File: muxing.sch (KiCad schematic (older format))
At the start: 10 parts, among them J10 Conn_01x06, J11 Conn_01x06

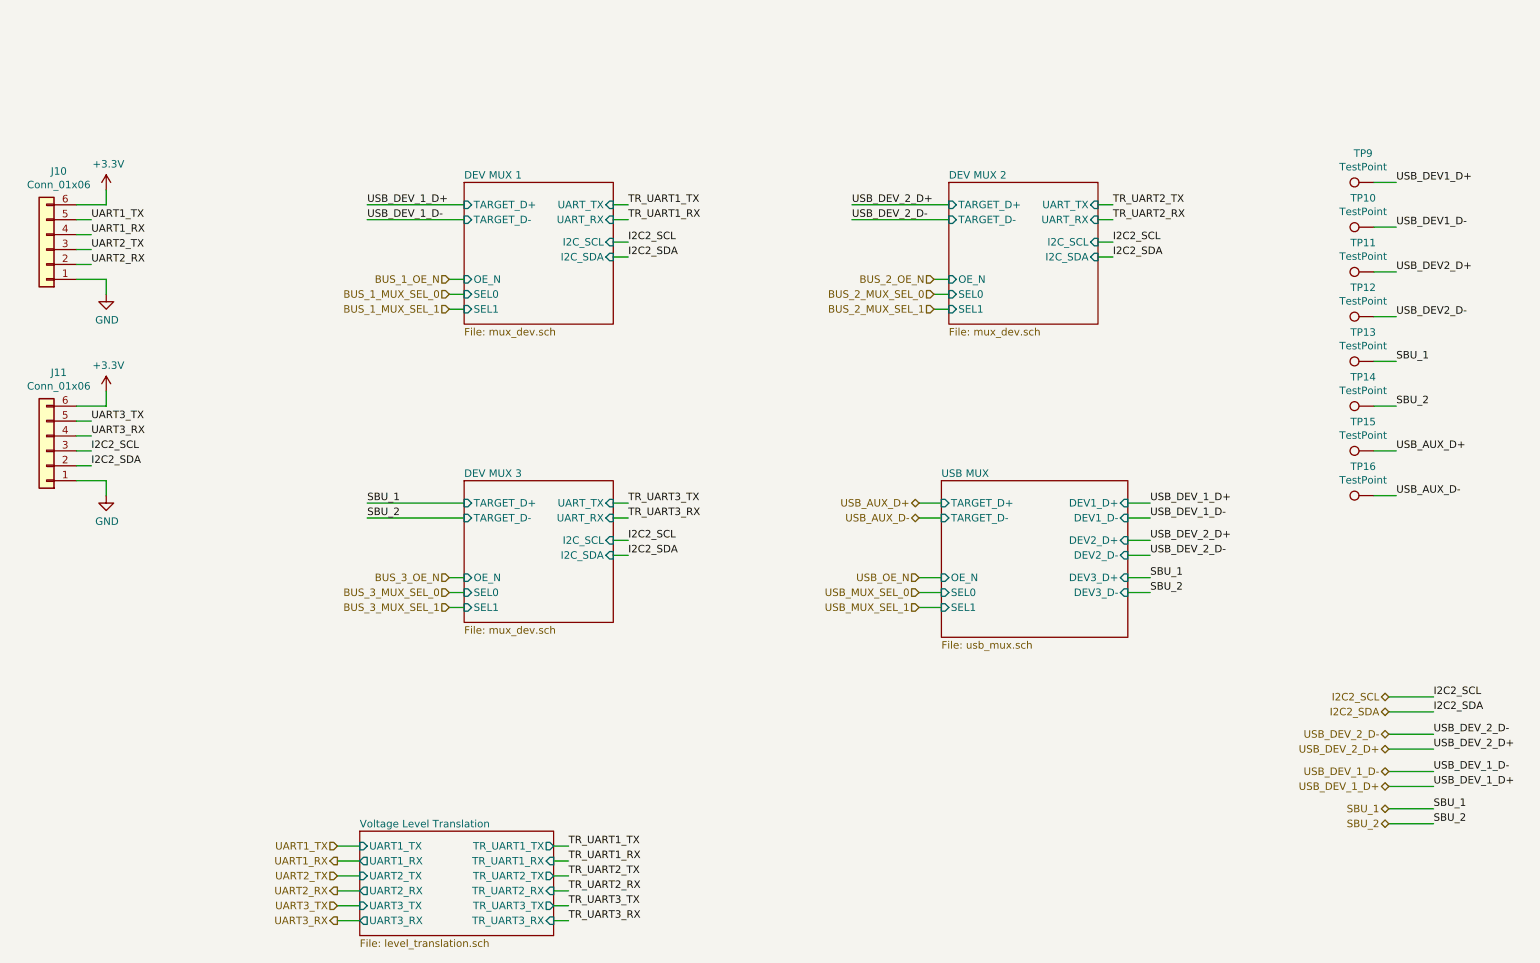
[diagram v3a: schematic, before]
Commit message: Replace MCU by something available in distributors
Given the current chip shortage the STM32F0 was not available from
JLCPCB. This one (STM32F411CE) is available in large quantities from
JLCPCB. Despite being much more powerful than the F0, it is still in the
price range and actually cheaper than the STM32F103C8T6... which I don't
understand...
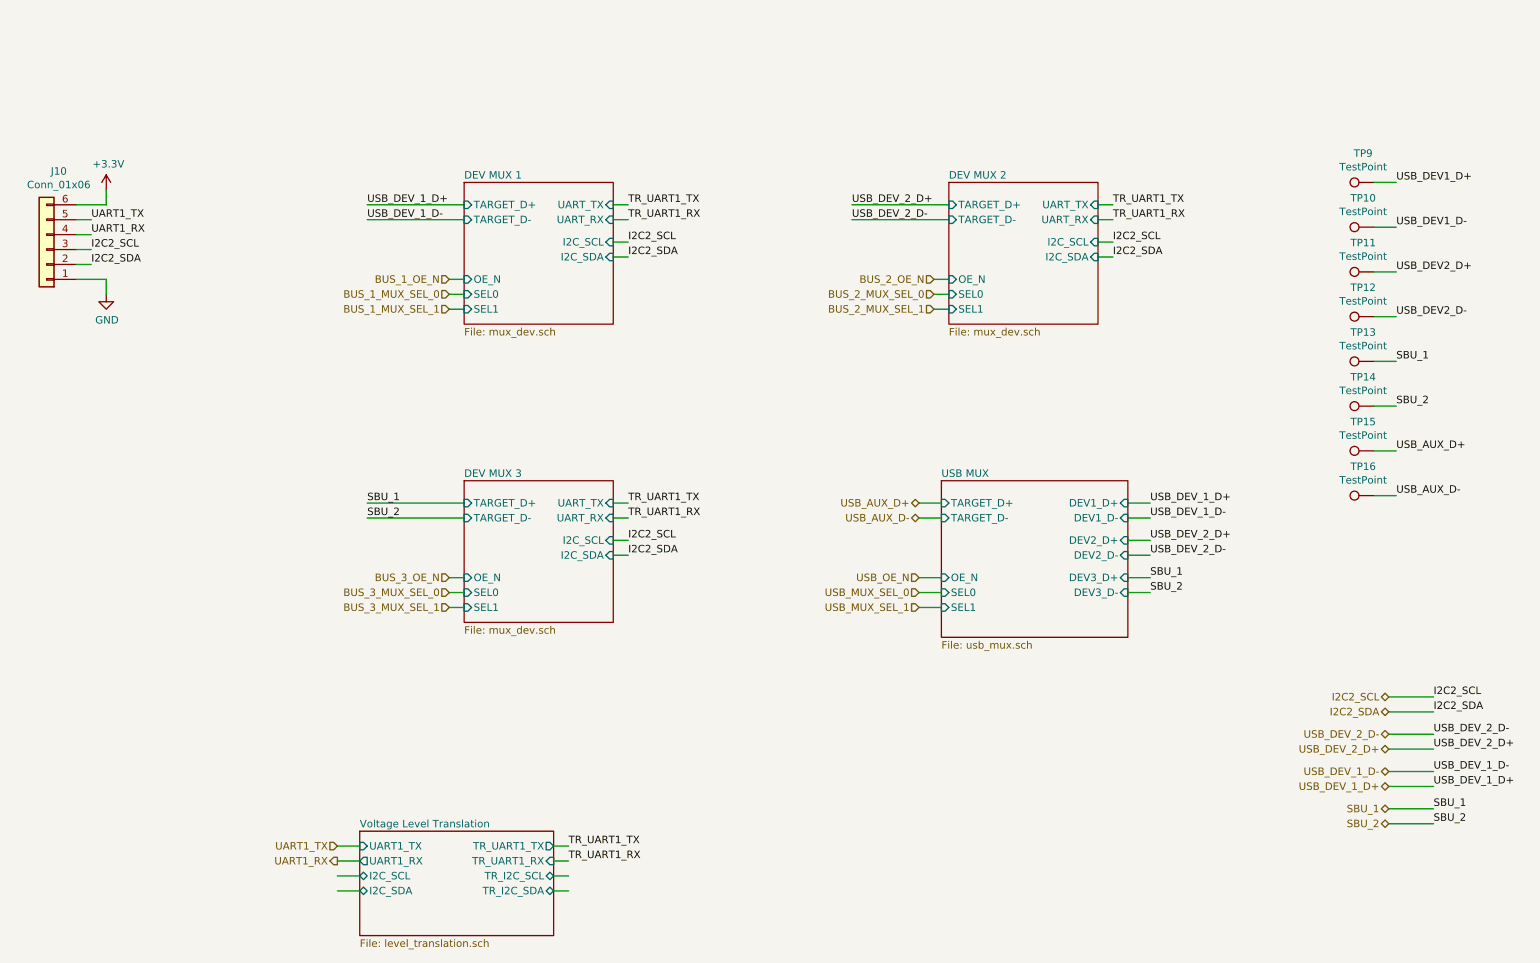
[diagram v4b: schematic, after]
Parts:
- removed J11: Conn_01x06, symbol Connector_Generic:Conn_01x06
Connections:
- net labels removed: TR_UART2_RX, TR_UART2_TX, TR_UART3_RX, TR_UART3_TX, UART2_RX, UART2_TX, UART3_RX, UART3_TX
- wire segments 82 -> 70
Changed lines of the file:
@@
 Wire Wire Line
 	7100 2250 6450 2250
-Text Label 8200 2150 0    50   ~ 0
-TR_UART2_TX
-Text Label 8200 2250 0    50   ~ 0
-TR_UART2_RX
 Wire Wire Line
 	8100 2150 8200 2150
@@
 Wire Wire Line
 	3850 4250 3200 4250
-Text Label 4950 4150 0    50   ~ 0
-TR_UART3_TX
-Text Label 4950 4250 0    50   ~ 0
-TR_UART3_RX
 Wire Wire Line
 	4850 4150 4950 4150
@@
 Text Label 4550 6550 0    50   ~ 0
 TR_UART1_RX
-Text Label 4550 6650 0    50   ~ 0
-TR_UART2_TX
-Text Label 4550 6750 0    50   ~ 0
-TR_UART2_RX
-Text Label 4550 6850 0    50   ~ 0
-TR_UART3_TX
-Text Label 4550 6950 0    50   ~ 0
-TR_UART3_RX
 Text HLabel 3750 4850 0    50   Input ~ 0
 BUS_3_MUX_SEL_1
@@
 F2 "UART1_TX" I L 3150 6450 50
 F3 "UART1_RX" O L 3150 6550 50
-F4 "UART2_TX" I L 3150 6650 50
-F5 "UART2_RX" O L 3150 6750 50
-F6 "UART3_TX" I L 3150 6850 50
-F7 "UART3_RX" O L 3150 6950 50
-F8 "TR_UART1_TX" O R 4450 6450 50
-F9 "TR_UART1_RX" I R 4450 6550 50
-F10 "TR_UART2_TX" O R 4450 6650 50
-F11 "TR_UART2_RX" I R 4450 6750 50
-F12 "TR_UART3_TX" O R 4450 6850 50
-F13 "TR_UART3_RX" I R 4450 6950 50
+F4 "TR_UART1_TX" O R 4450 6450 50
+F5 "TR_UART1_RX" I R 4450 6550 50
+F6 "I2C_SCL" B L 3150 6650 50
+F7 "I2C_SDA" B L 3150 6750 50
+F8 "TR_I2C_SCL" B R 4450 6650 50
+F9 "TR_I2C_SDA" B R 4450 6750 50
 $EndSheet
 Wire Wire Line
@@
 Wire Wire Line
 	4550 6750 4450 6750
-Wire Wire Line
-	4450 6850 4550 6850
-Wire Wire Line
-	4550 6950 4450 6950
 $Sheet
 S 7050 4000 1250 1050
@@
 Text HLabel 3000 6550 0    50   Output ~ 0
 UART1_RX
-Text HLabel 3000 6650 0    50   Input ~ 0
-UART2_TX
-Text HLabel 3000 6750 0    50   Output ~ 0
-UART2_RX
-Text HLabel 3000 6850 0    50   Input ~ 0
-UART3_TX
-Text HLabel 3000 6950 0    50   Output ~ 0
-UART3_RX
 Wire Wire Line
 	3000 6450 3150 6450
@@
 Wire Wire Line
 	3150 6750 3000 6750
-Wire Wire Line
-	3000 6850 3150 6850
-Wire Wire Line
-	3150 6950 3000 6950
 Text HLabel 6900 4150 0    50   BiDi ~ 0
 USB_AUX_D+
@@
 Text Label 1350 2350 0    50   ~ 0
 UART1_RX
-Text Label 1350 2450 0    50   ~ 0
-UART2_TX
-Text Label 1350 2550 0    50   ~ 0
-UART2_RX
-Text Label 1350 3600 0    50   ~ 0
-UART3_TX
-Text Label 1350 3700 0    50   ~ 0
-UART3_RX
 $Comp
 L power:+3.3V #PWR019
@@
 	1250 2550 1350 2550
 Wire Wire Line
-	1350 3600 1250 3600
-Wire Wire Line
-	1250 3700 1350 3700
-Wire Wire Line
 	1250 2650 1450 2650
 Wire Wire Line
@@
 Wire Wire Line
 	1450 2150 1250 2150
-$Comp
-L power:+3.3V #PWR023
-U 1 1 61A3EEDE
-P 1450 3400
-F 0 "#PWR023" H 1450 3250 50  0001 C CNN
-F 1 "+3.3V" H 1465 3573 50  0000 C CNN
-F 2 "" H 1450 3400 50  0001 C CNN
-F 3 "" H 1450 3400 50  0001 C CNN
-	1    1450 3400
-	1    0    0    -1
-$EndComp
-$Comp
-L power:GND #PWR025
-U 1 1 61A3EEE4
-P 1450 4100
-F 0 "#PWR025" H 1450 3850 50  0001 C CNN
-F 1 "GND" H 1455 3927 50  0000 C CNN
-F 2 "" H 1450 4100 50  0001 C CNN
-F 3 "" H 1450 4100 50  0001 C CNN
-	1    1450 4100
-	1    0    0    -1
-$EndComp
-Wire Wire Line
-	1250 4000 1450 4000
-Wire Wire Line
-	1450 4000 1450 4100
-Wire Wire Line
-	1450 3400 1450 3500
-Wire Wire Line
-	1450 3500 1250 3500
-$Comp
-L Connector_Generic:Conn_01x06 J11
-U 1 1 61A4FE69
-P 1050 3800
-F 0 "J11" H 968 3275 50  0000 C CNN
-F 1 "Conn_01x06" H 968 3366 50  0000 C CNN
-F 2 "" H 1050 3800 50  0001 C CNN
-F 3 "~" H 1050 3800 50  0001 C CNN
-	1    1050 3800
-	-1   0    0    1
-$EndComp
 $Comp
 L Connector_Generic:Conn_01x06 J10
@@
 	-1   0    0    1
 $EndComp
-Text Label 1350 3800 0    50   ~ 0
+Text Label 1350 2450 0    50   ~ 0
 I2C2_SCL
-Text Label 1350 3900 0    50   ~ 0
+Text Label 1350 2550 0    50   ~ 0
 I2C2_SDA
-Wire Wire Line
-	1350 3800 1250 3800
-Wire Wire Line
-	1250 3900 1350 3900
 $Comp
 L Connector:TestPoint TP9
@@
 Wire Wire Line
 	9950 4100 10100 4100
+Text Label 8200 2150 0    50   ~ 0
+TR_UART1_TX
+Text Label 8200 2250 0    50   ~ 0
+TR_UART1_RX
+Text Label 4950 4150 0    50   ~ 0
+TR_UART1_TX
+Text Label 4950 4250 0    50   ~ 0
+TR_UART1_RX
 $EndSCHEMATC
